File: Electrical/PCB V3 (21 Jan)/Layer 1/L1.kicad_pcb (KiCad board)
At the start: 2 copper layers, 178 x 170 mm, 192 parts, among them J1 Conn_01x04, J2 Conn_01x02, Q2 STP75NF75, Q4 IRLML6344TRPBF, U1 LM2587S-ADJ, U2 CD74HC4067SM, U3 CD74HC4067SM, U4 XT30UPB-M, U5 113991054

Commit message: fixed l1 jst position
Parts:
- moved J1 5.00 mm to (188.8, 92.8)
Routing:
- net /L1 TX: track 17.9 -> 22.1 mm
- net /L1 RX: track 42.8 -> 46.9 mm
- net +3V3: track 121.5 -> 123.0 mm
- net GND: vias 271 -> 273

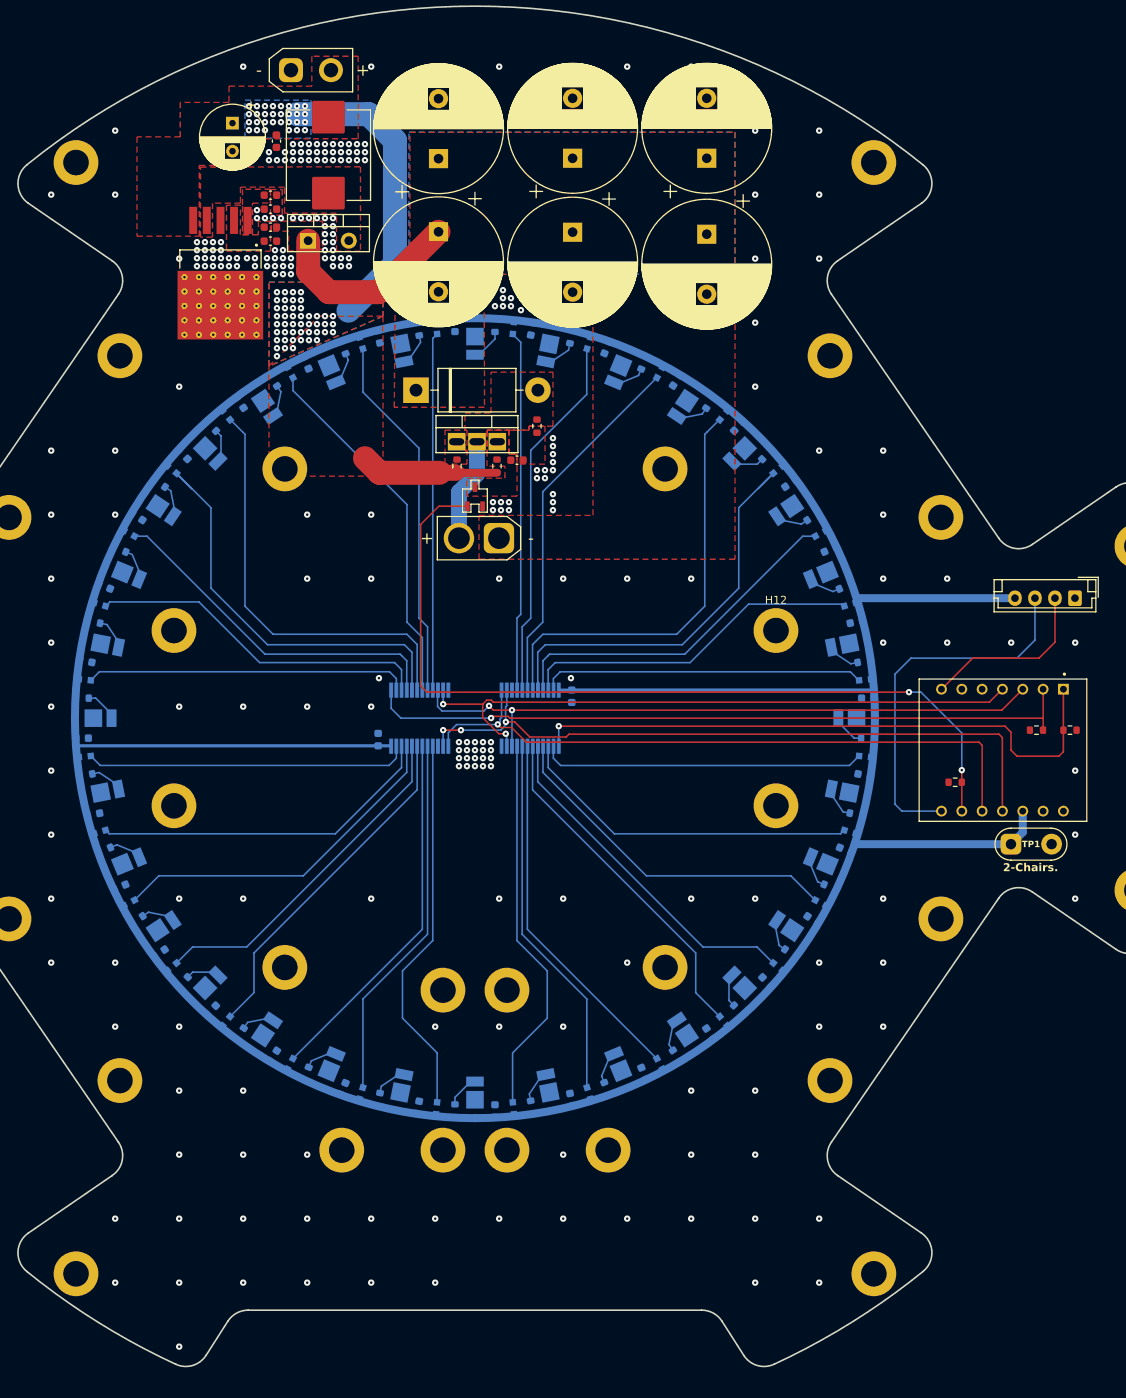
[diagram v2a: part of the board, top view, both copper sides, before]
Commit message: fixed l1 and l3
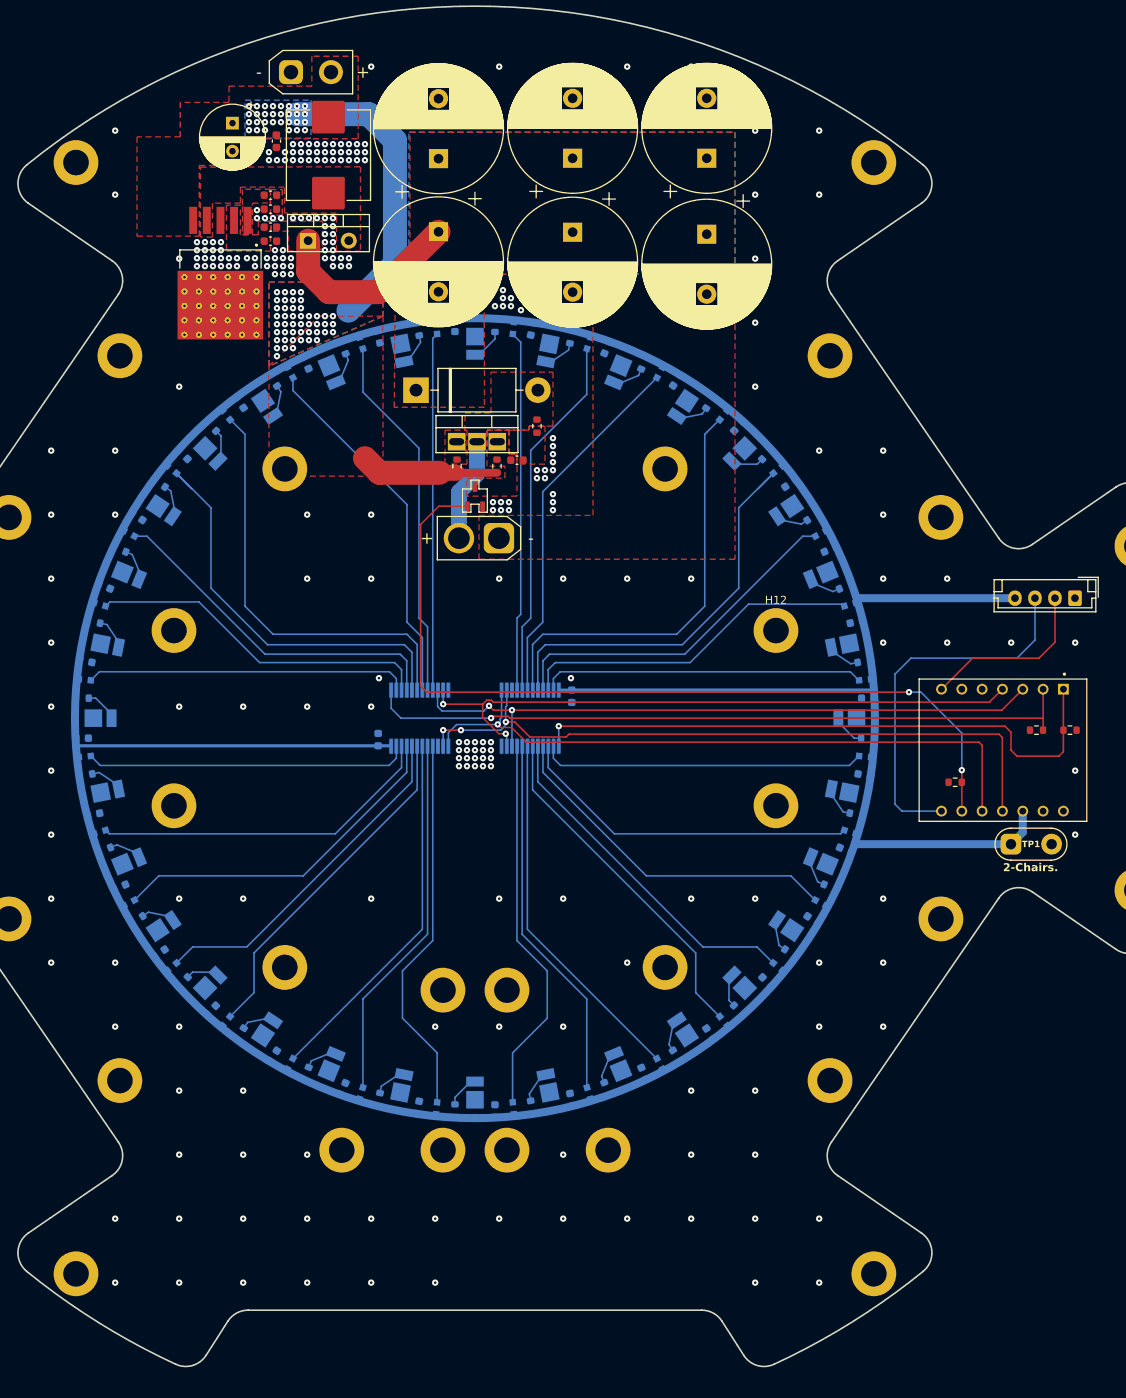
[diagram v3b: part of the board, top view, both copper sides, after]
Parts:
- moved J2 0.25 mm to (90.8, 27.0)
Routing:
- net GND: vias 273 -> 268

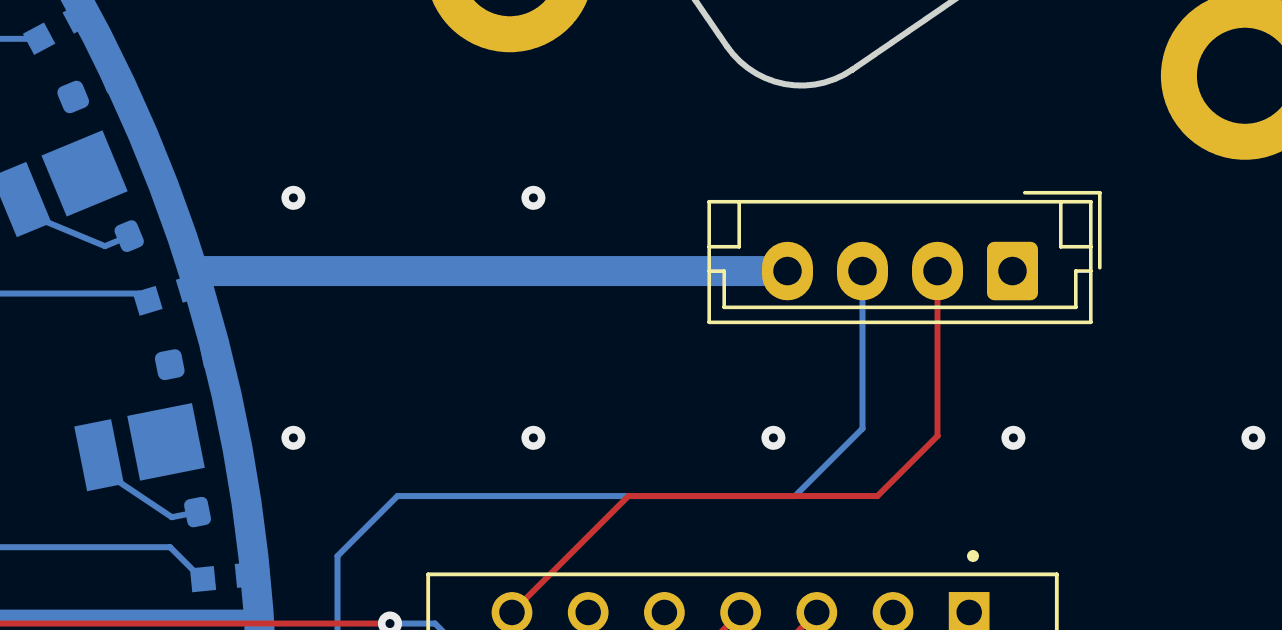
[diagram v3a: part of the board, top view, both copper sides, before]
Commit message: change l1 1x4jst pos
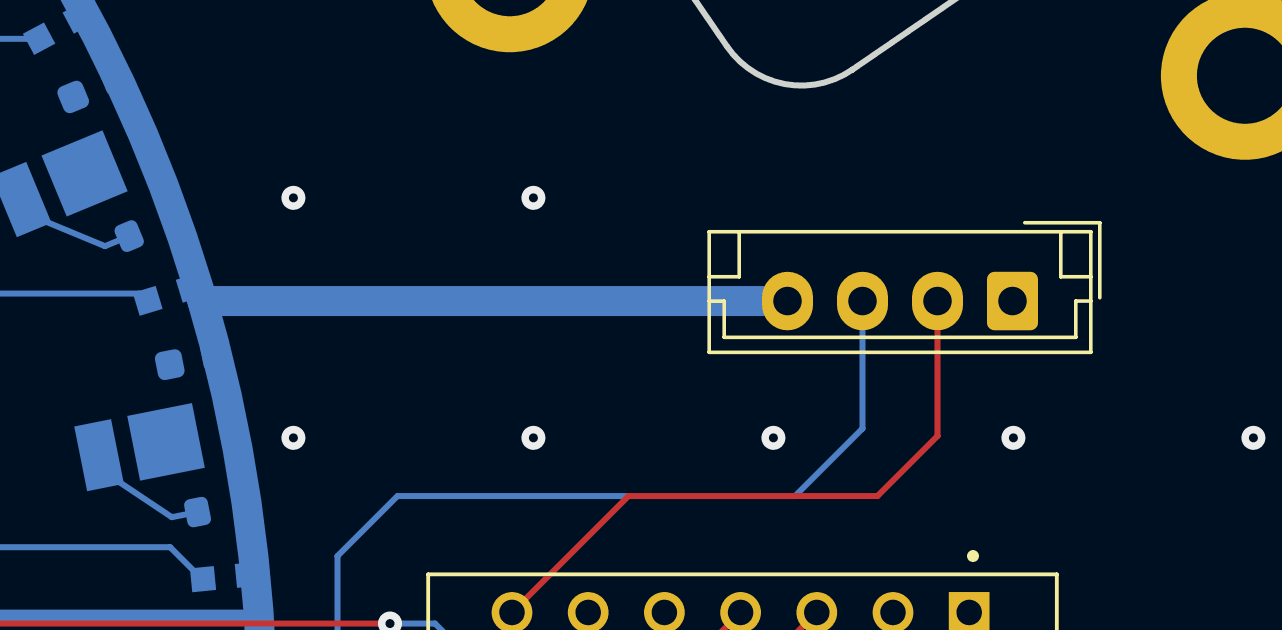
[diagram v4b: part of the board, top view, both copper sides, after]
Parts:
- moved J1 1.00 mm to (188.8, 93.8)
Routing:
- net /L1 TX: track 22.1 -> 21.1 mm
- net /L1 RX: track 46.9 -> 45.9 mm
